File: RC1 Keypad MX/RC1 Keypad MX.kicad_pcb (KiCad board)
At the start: 2 copper layers, 73 x 122.6 mm, 26 parts, among them J1 KB, SW1 Ø, SW10 3, SW11 A, SW12 DA, SW13 4, SW14 B, SW15 +, SW16 5, SW17 C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

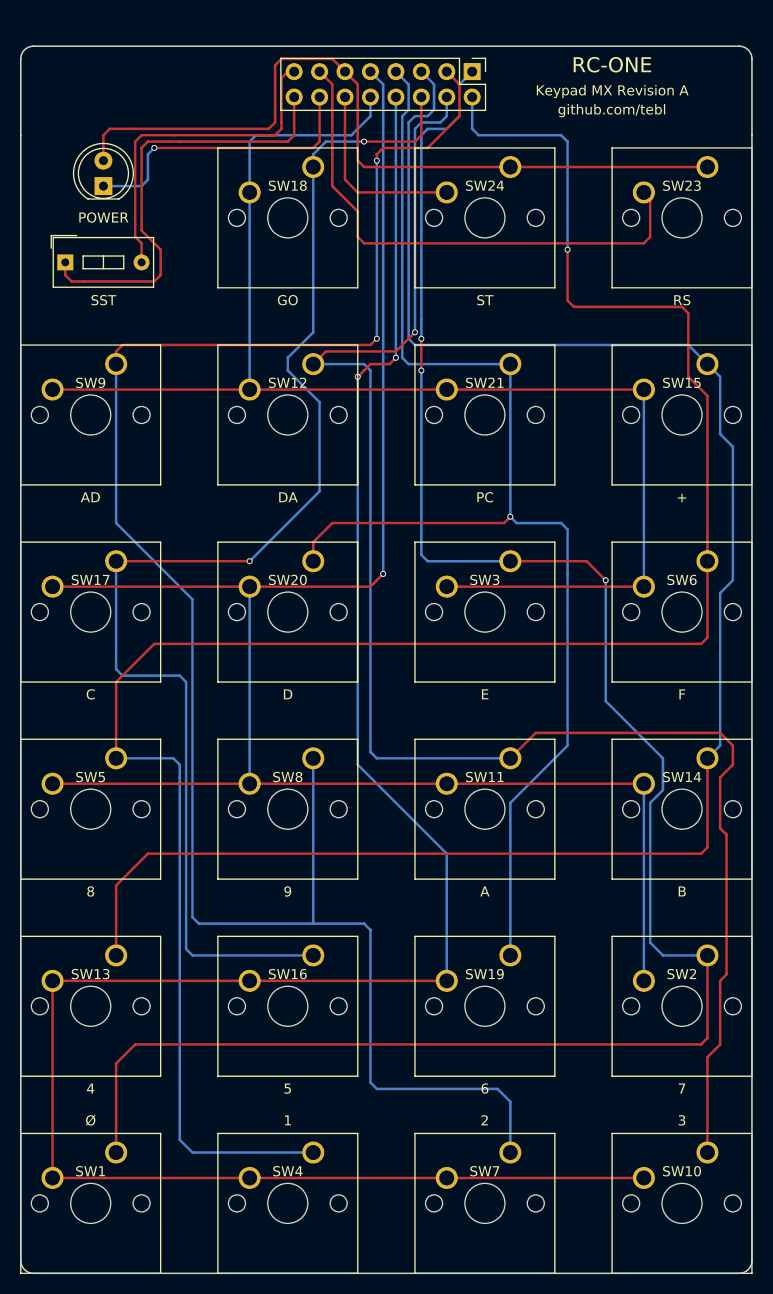
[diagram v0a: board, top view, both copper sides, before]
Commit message: Keypad MX SST moved to match original keypad layout
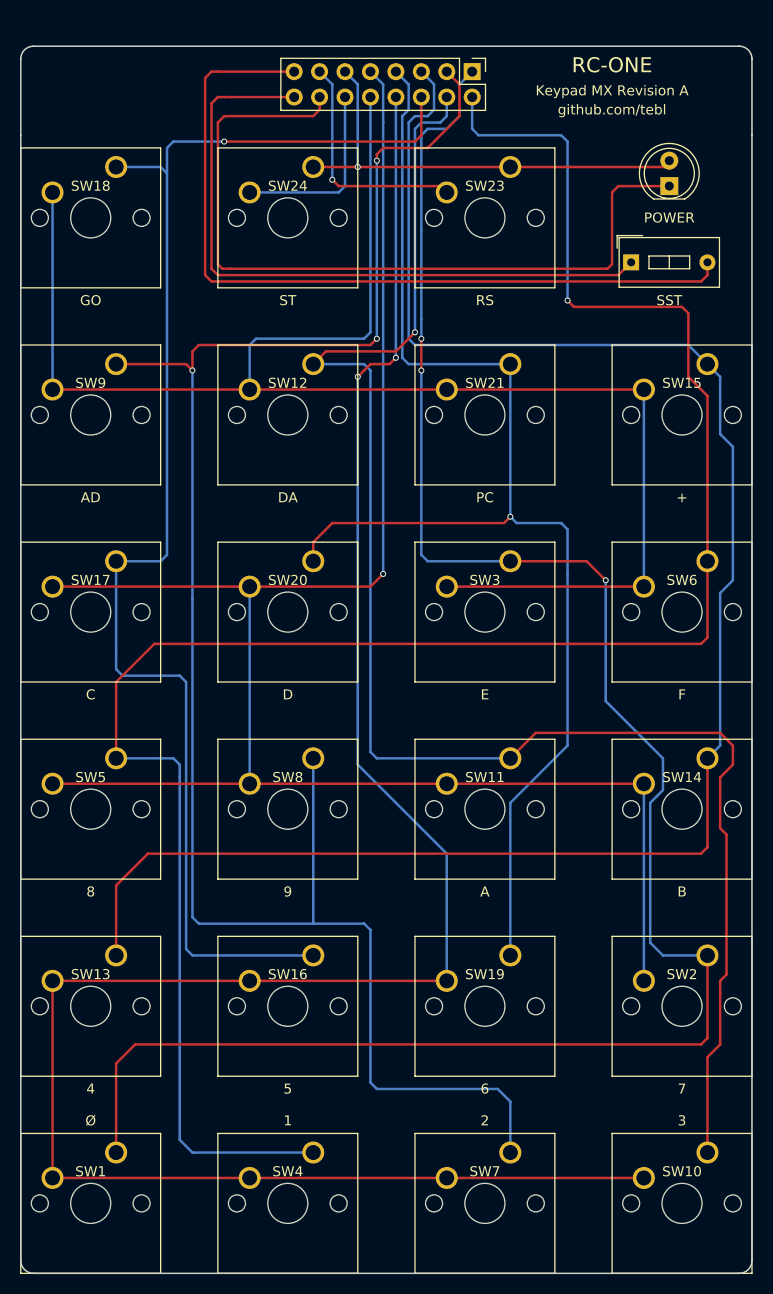
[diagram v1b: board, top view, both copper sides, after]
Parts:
- moved D1 56.5 mm to (149.2, 69.2)
- moved SW22 56.5 mm to (145.4, 76.8)
- moved SW18 19.7 mm to (94.0, 67.3)
- moved SW23 19.7 mm to (133.3, 67.3)
- moved SW24 19.7 mm to (113.7, 67.3)
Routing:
- net /LED: track 29.5 -> 79.4 mm, vias 1 -> 0
- net /SST_OUT: track 34.1 -> 80.8 mm
- net /VCC: track 78.3 -> 45.9 mm, vias 0 -> 1
- net /RS: track 52.5 -> 23.3 mm, vias 0 -> 1
- net /SST_IN: track 44.4 -> 67.7 mm
- net /ROW_0: track 138.2 -> 158.6 mm
- net /2A1: track 132.6 -> 139.0 mm, vias 2 -> 1
- net /2A4: track 189.3 -> 186.5 mm, vias 2 -> 3

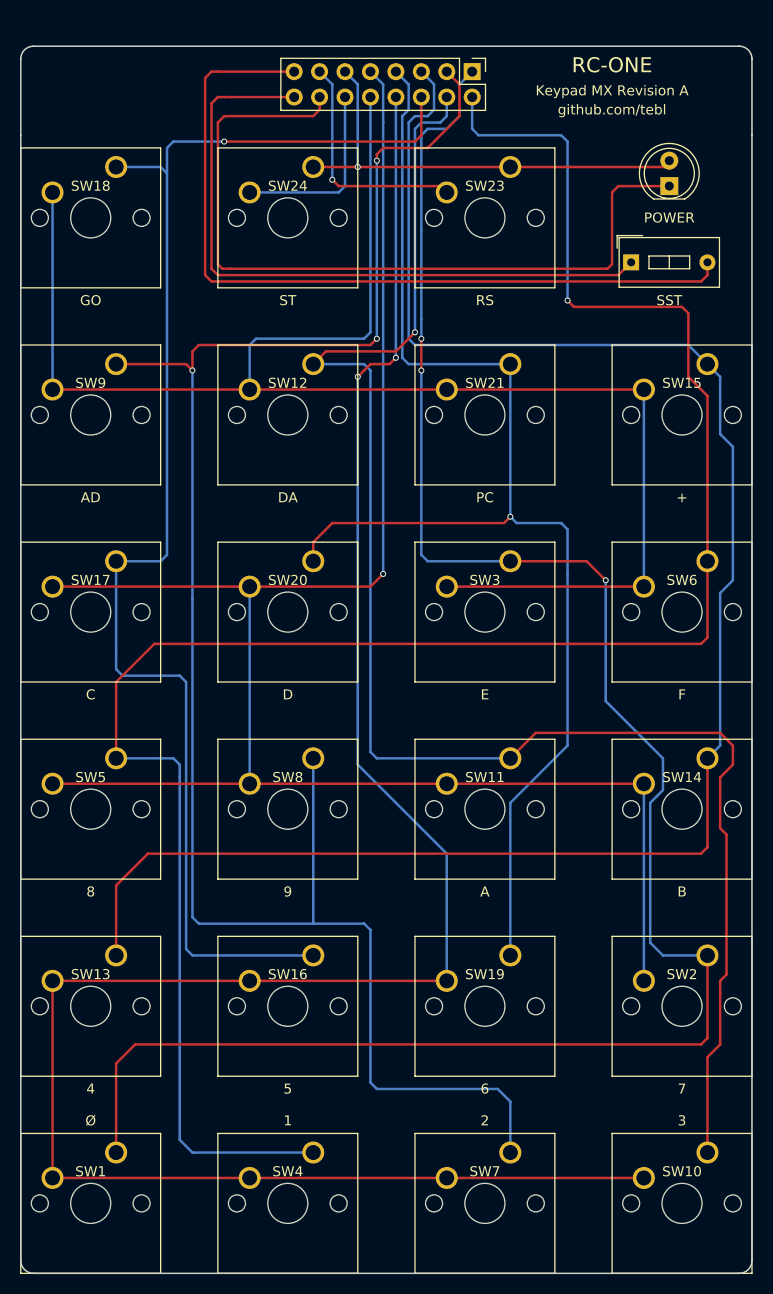
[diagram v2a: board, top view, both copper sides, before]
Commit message: MX Keypad now matches Commodore Kim-1
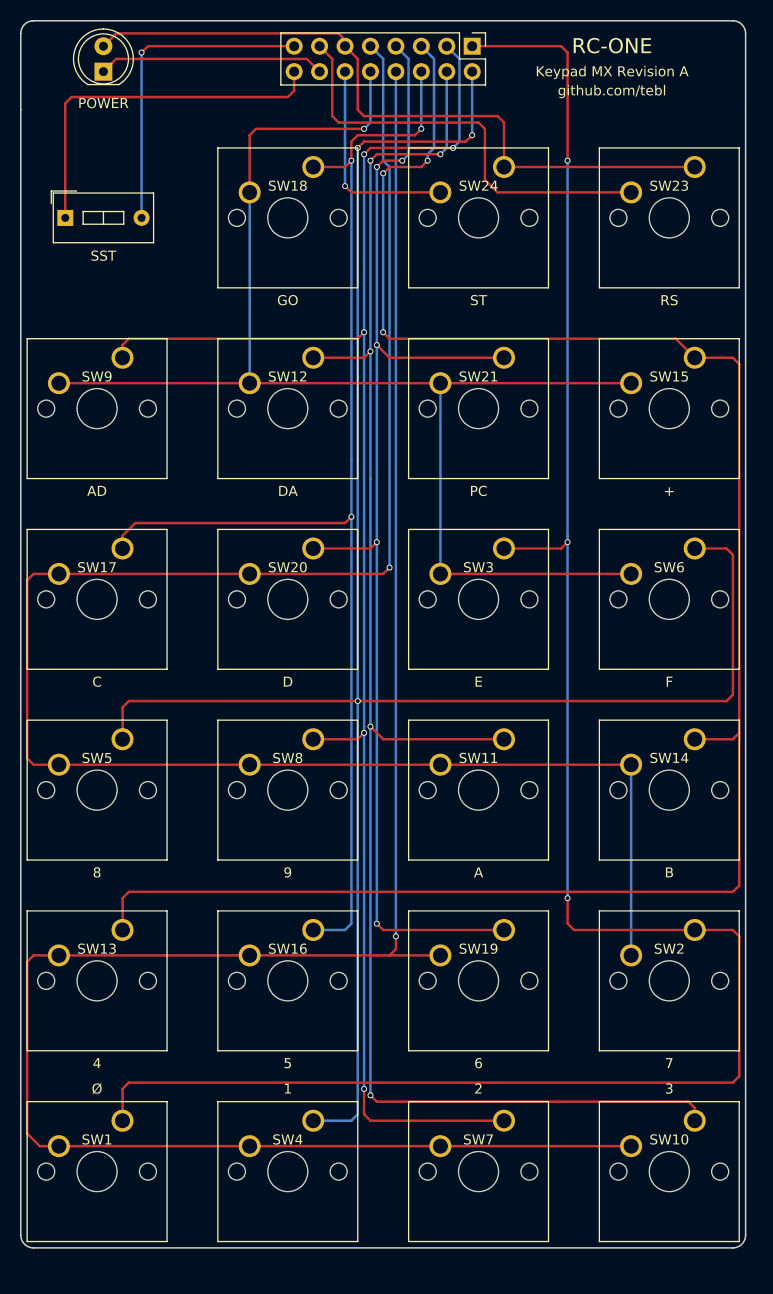
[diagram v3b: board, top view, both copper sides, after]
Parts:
- moved D1 57.7 mm to (92.7, 57.8)
- moved SW22 56.7 mm to (88.9, 72.4)
- moved SW18 19.7 mm to (113.7, 67.3)
- moved SW24 19.0 mm to (132.7, 67.3)
- moved SW23 18.4 mm to (151.8, 67.3)
- moved SW10 3.42 mm to (151.8, 162.6)
- moved SW1 3.24 mm to (94.6, 162.6)
- moved SW7 3.24 mm to (132.7, 162.6)
- moved SW4 3.18 mm to (113.7, 162.6)
- moved SW2 2.84 mm to (151.8, 143.5)
- moved SW13 2.62 mm to (94.6, 143.5)
- moved SW19 2.62 mm to (132.7, 143.5)
- moved SW16 2.54 mm to (113.7, 143.5)
- moved J1 2.54 mm to (129.5, 55.2)
- moved SW14 2.29 mm to (151.8, 124.5)
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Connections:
- net /2A0 renamed /PA0
- net /2A1 renamed /PA1
- net /2A2 renamed /PA2
- net /2A3 renamed /PA3
- net /2A4 renamed /PA4
- net /2A5 renamed /PA5
- net /2A6 renamed /PA6
- net /LED renamed Net-(D1-Pad1)
- net /ROW_0 renamed /ROW2
- net /ROW_1 renamed /ROW1
- net /ROW_2 renamed /ROW0
- net /RS renamed Net-(J1-Pad13)
- net /SST_IN renamed Net-(J1-Pad16)
- net /SST_OUT renamed Net-(J1-Pad15)
- net /ST renamed Net-(J1-Pad12)
- net /VCC renamed Net-(D1-Pad2)
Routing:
- net Net-(D1-Pad1): track 79.4 -> 22.6 mm
- net Net-(J1-Pad15): track 80.8 -> 32.0 mm, vias 0 -> 1
- net Net-(J1-Pad16): track 67.7 -> 36.7 mm
- net Net-(D1-Pad2): track 45.9 -> 71.1 mm, vias 1 -> 0
- net /PA4: track 186.5 -> 161.5 mm, vias 3 -> 5
- net /ROW2: track 158.6 -> 137.7 mm, vias 0 -> 1
- net Net-(J1-Pad13): track 23.3 -> 43.5 mm, vias 1 -> 0
- net /PA1: track 139.0 -> 124.4 mm, vias 1 -> 3
- net /PA2: track 177.9 -> 192.0 mm, vias 0 -> 3
- net /PA6: track 193.5 -> 200.3 mm
- net /PA0: track 129.5 -> 123.4 mm, vias 1 -> 5
- net /ROW0: track 212.8 -> 208.1 mm, vias 2 -> 1
- net /ROW1: track 182.7 -> 187.0 mm
- net Net-(J1-Pad12): track 18.7 -> 21.2 mm, vias 0 -> 1
- net /PA3: track 161.7 -> 163.1 mm, vias 1 -> 5
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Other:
- board size 73 x 122.6 mm -> 72.4 x 122.6 mm
